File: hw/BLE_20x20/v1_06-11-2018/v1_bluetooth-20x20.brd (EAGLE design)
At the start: 26 x 22 mm, 18 parts, among them J2 header, U1 NRF52832

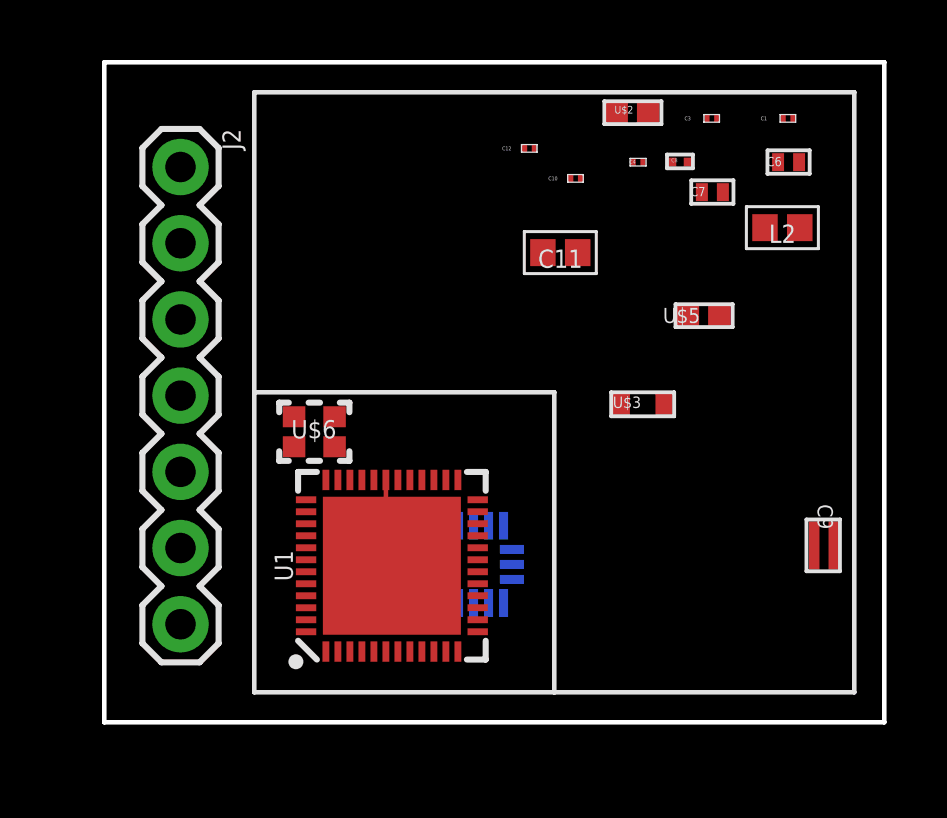
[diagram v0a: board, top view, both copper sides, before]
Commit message: working on ble 20x20 completing airwires
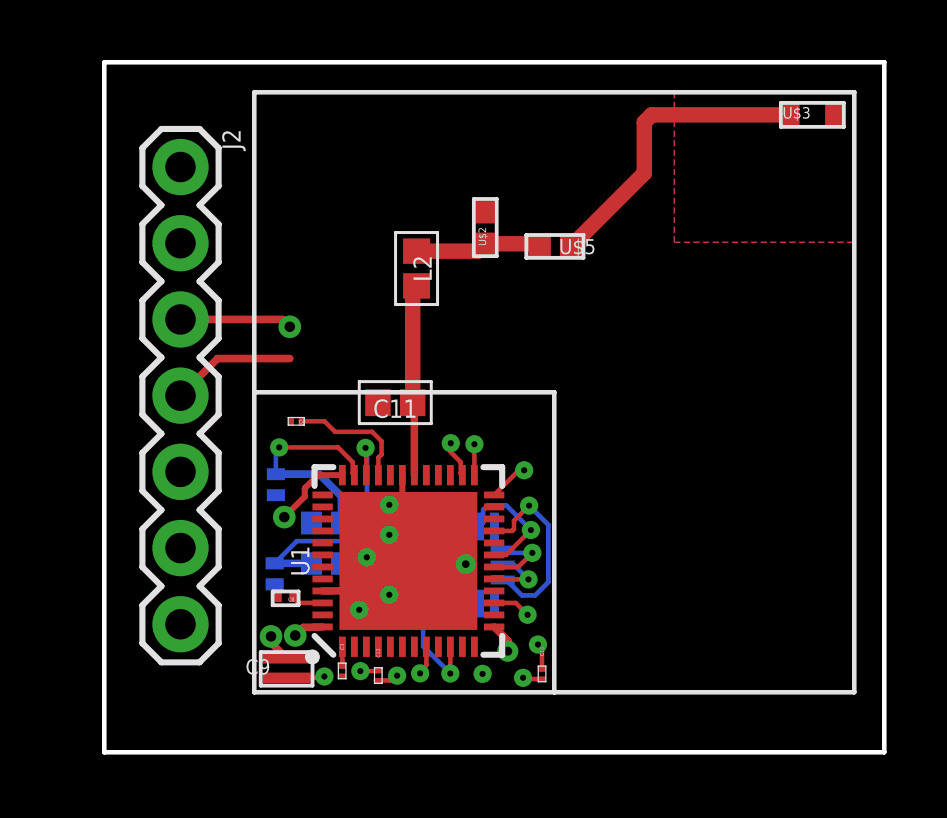
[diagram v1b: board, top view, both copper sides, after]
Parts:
- moved C3 22.1 mm to (2.93, 0.72), turned to 270 degrees
- moved C6 20.2 mm to (0.72, 6.97), flipped to the bottom, turned to 90 degrees
- moved C8 19.6 mm to (0.99, 3.16), turned to 180 degrees
- moved C7 19.4 mm to (0.68, 4.00), flipped to the bottom, turned to 90 degrees
- moved C9 18.3 mm to (1.18, 0.88), turned to 90 degrees
- moved C12 18.3 mm to (4.13, 0.56), turned to 270 degrees
- moved C1 17.4 mm to (5.83, 6.45), flipped to the bottom, turned to 180 degrees
- moved C10 16.5 mm to (9.59, 0.62), turned to 270 degrees
- moved C4 14.3 mm to (1.41, 9.03), turned to 180 degrees
- moved L2 12.3 mm to (5.41, 14.1), turned to 90 degrees
- moved U$3 11.2 mm to (17.6, 18.8)
- moved C11 7.43 mm to (4.70, 9.66)
- moved U$2 6.60 mm to (7.70, 16.6), turned to 90 degrees
- moved U$5 5.14 mm to (10.2, 14.9), turned to 180 degrees
- moved U$6 3.95 mm to (1.44, 3.81), flipped to the bottom, turned to 90 degrees
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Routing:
- net SWDIO-QFAA: track 0.00 -> 15.7 mm, vias 0 -> 1
- net SWDCLK-QFAA: track 0.00 -> 13.9 mm, vias 0 -> 1
- net P0.12-QFAA: track 0.00 -> 13.3 mm, vias 0 -> 1
- net RESET-QFAA: track 0.00 -> 12.8 mm, vias 0 -> 1
- net GND: track 3.44 -> 16.2 mm, vias 0 -> 9
- net P0.06-QFAA: track 0.00 -> 11.0 mm, vias 0 -> 1
- net VDD: track 0.00 -> 10.9 mm, vias 0 -> 8
- net N$2: track 0.00 -> 10.1 mm
- net XC1-QFAA: track 0.00 -> 8.42 mm, vias 0 -> 1
- net ADXL_POWER-QFAA: track 0.00 -> 8.31 mm, vias 0 -> 1
- net XC2-QFAA: track 0.00 -> 7.43 mm, vias 0 -> 1
- net CS-QFAA: track 0.00 -> 6.41 mm, vias 0 -> 1
- net ANT-QFAA: track 0.00 -> 6.38 mm
- net N$1: track 0.00 -> 4.24 mm
- net SCLK-QFAA: track 0.00 -> 4.16 mm, vias 0 -> 1
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- added copper zone on layer 1, net GND
- added copper zone on layer 16, net GND
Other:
- board size 26 x 22 mm -> 26 x 23 mm

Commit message: finished pcb, added 112 tsilk
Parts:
- moved U$3 0.41 mm to (17.2, 18.7)
- moved U$2 0.41 mm to (7.30, 16.5)
- moved U$5 0.41 mm to (9.81, 14.8)
- moved U$1 0.41 mm to (6.61, 4.14)
- moved U1 0.41 mm to (4.74, 4.28)
- moved C1 0.41 mm to (5.43, 6.35)
- moved C10 0.41 mm to (9.19, 0.52)
- moved C11 0.41 mm to (4.30, 9.56)
- moved J2 0.41 mm to (-2.86, 17.4)
- moved L2 0.41 mm to (5.01, 14.0)
- moved C4 0.41 mm to (1.01, 8.93)
- moved C8 0.41 mm to (0.59, 3.06)
- moved C9 0.41 mm to (0.78, 0.78)
- moved C6 0.41 mm to (0.32, 6.87)
- moved C7 0.41 mm to (0.28, 3.90)
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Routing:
- net N$3: track 0.00 -> 7.70 mm
- net GND: vias 9 -> 10
- net VDD: vias 8 -> 9
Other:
- board size 26 x 23 mm -> 27 x 23 mm
- board text added: "GND"
- board text added: "P0.06"
- board text added: "P0.12"
- board text added: "RESET"
- board text added: "SWDCLK"
- board text added: "SWDIO"
- board text added: "VDD"
